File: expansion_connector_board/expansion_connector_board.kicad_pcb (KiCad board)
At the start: 2 copper layers, 154 x 93.2 mm, 20 parts, among them J1 POWER RELAY, J12 Conn_02x17_Top_Bottom, J13 POWER RELAY, J14 Conn_02x17_Top_Bottom, J19 MEGA65 R4+ Analog Audio Header, J2 GPIO Breakout, J3 693063020911, J4 MEGA65 JTAG+SERIAL HEADER, J5 EXP BOARD TE0790 RELAY, J6 Helper/Peripheral UART Interf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, J7 Conn_01x04, SW1 WRITE REQUEST PUSH BUTTON, U1 74CBTLV3257

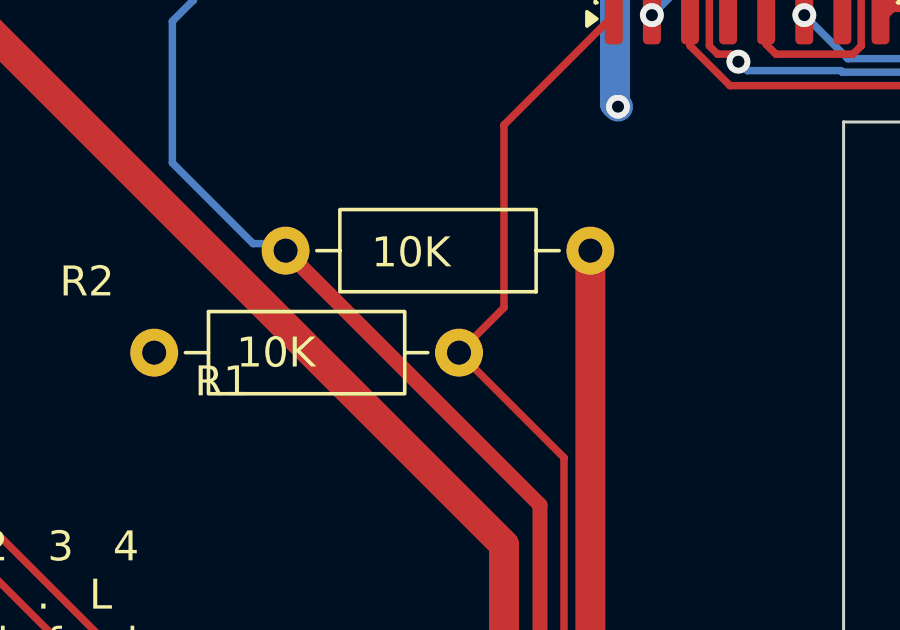
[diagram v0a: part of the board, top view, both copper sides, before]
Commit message: Minor changes from DRC.
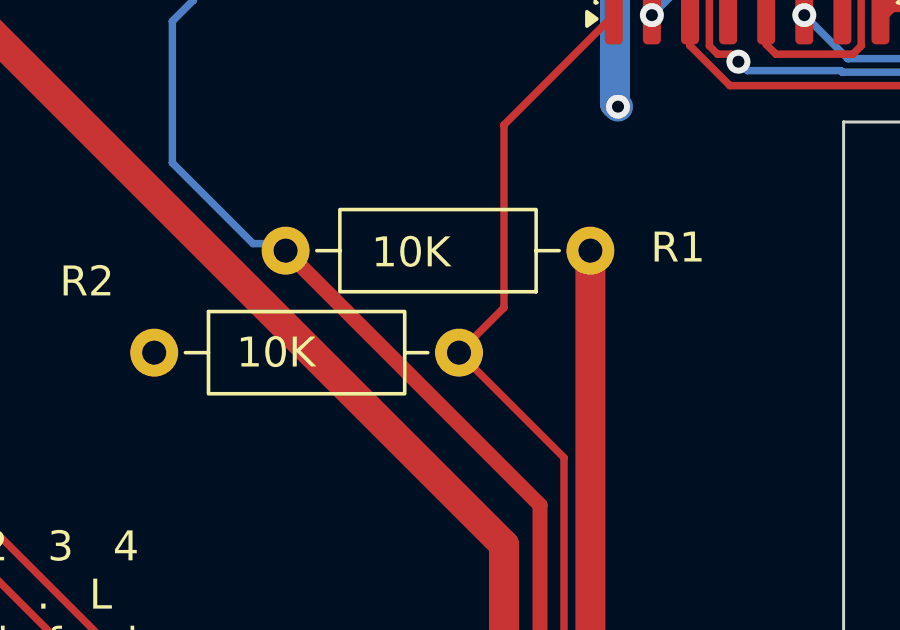
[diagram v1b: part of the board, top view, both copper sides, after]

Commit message: Add in the temodule and the step layers
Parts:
- added STACK_PREVIEW: , StackPreview:STACK_PREVIEW, F.Cu at (0.00, 0.00)
- J1, J13: footprint Connector_PinHeader_2.54mm:PinHeader_1x04_P2.54mm_Vertical -> Connector_PinSocket_2.54mm:PinSocket_1x04_P2.54mm_Vertical; moved to B.Cu
- J12, J14: footprint Connector_PinHeader_2.54mm:PinHeader_2x17_P2.54mm_Vertical -> Connector_PinSocket_2.54mm:PinSocket_2x17_P2.54mm_Vertical; moved to B.Cu
- J19: footprint Connector_PinHeader_2.54mm:PinHeader_2x05_P2.54mm_Vertical -> Connector_PinSocket_2.54mm:PinSocket_2x05_P2.54mm_Vertical; moved to B.Cu
- J4, J5: footprint Connector_PinHeader_2.54mm:PinHeader_2x06_P2.54mm_Vertical -> Connector_PinSocket_2.54mm:PinSocket_2x06_P2.54mm_Vertical; moved to B.Cu
- J6: footprint Connector_PinHeader_2.54mm:PinHeader_1x08_P2.54mm_Vertical -> Connector_PinSocket_2.54mm:PinSocket_1x08_P2.54mm_Vertical; moved to B.Cu
- turned J1 to 180 degrees
- turned J12 to 0 degrees
- turned J13 to 180 degrees
- turned J14 to 0 degrees
- turned J19 to 90 degrees
- turned J4 to 90 degrees
- turned J5 to 90 degrees
- turned J6 to -90 degrees
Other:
- outline, holes or cut-outs redrawn
